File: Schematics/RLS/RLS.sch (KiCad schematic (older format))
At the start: 3 parts

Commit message: Updated schematic
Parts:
- added 1.5A: Fuse_Small2, symbol Fuse_Small
- added 1A: Fuse_Small3, symbol Fuse_Small
- added 4A: Fuse_Small1, symbol Fuse_Small
- added Arduino_Connector: ARDUINO_MEGA_SHIELD, symbol ARDUINO_MEGA_SHIELD
- added Logic_Analyzer_2: CONN_02X20, symbol CONN_02X20
- added Power_Supply: DIN_5, symbol DIN_5
- added R1, R10, R2, R3, R4, R5, R6, R7, R8, R9: 4.7K, symbol R
- added U1: ULN2803A, symbol ULN2803A
- added Voltmeter: CONN_01X10, symbol CONN_01X10
- gave numbers to parts that had none: 2
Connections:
- net labels added: AA12, AA13, AA14, AA15, AD10, AD11, AD12, AD13, AD22, AD23, AD24, AD25, AD26, AD27, AD28, AD29, AD30, AD31, AD32, AD33, AD34, AD35, AD36, AD37, AD38, AD39, AD4, AD40, AD41, AD42, AD43, AD44, AD45, AD46, AD47, AD5, AD6, AD7, AD8, AD9, GNDA, GNDD, L1CLK1, L1CLK2, L1D0, L1D1, L1D10, L1D11, L1D12, L1D13, L1D14, L1D15, L1D16, L1D17, L1D18, L1D19, L1D2, L1D20, L1D21, L1D22, L1D23, L1D24, L1D25, L1D26, L1D27, L1D28, L1D29, L1D3, L1D30, L1D31, L1D4, L1D5, L1D6, L1D7, L1D8, L1D9, L1GND, L2CLK1, L2CLK2, L2D0, L2D1, L2D10, L2D11, L2D12, L2D13, L2D14, L2D15, L2D16, L2D17, L2D18, L2D19, L2D2, L2D20, L2D21, L2D22, L2D23, L2D24, L2D25, L2D26, L2D27, L2D28, L2D29, L2D3, L2D30, L2D31, L2D4, L2D5, L2D6, L2D7, L2D8, L2D9, L2GND, RLY1, RLY2, SCL, SDA
- net labels removed: A14, A15, CLK1, CLK2, D0, D1, D10, D11, D12, D13, D14, D15, D16, D17, D18, D19, D2, D20, D21, D22, D23, D24, D25, D26, D27, D28, D29, D3, D30, D31, D32, D33, D34, D35, D36, D37, D38, D39, D4, D40, D41, D42, D43, D44, D45, D46, D47, D5, D6, D7, D8, D9, GND
- wire segments 0 -> 53
- no-connect marks 0 -> 15
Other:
- moved on the sheet: Arduino_Connector, BoardID_Regulator_Scope_Gen

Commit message: 06-23-2017 Update
Updated the scope probe network to it's own screen
Changed the connector setup
Fixed mirrored logic analyzer pins
Created voltage divider network for voltmeter
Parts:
- removed R1, R2: 4.7K, symbol R
- removed U1: ULN2803A, symbol ULN2803A
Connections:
- net labels added: VD01, VD02, VD03
- net labels removed: RLY1, RLY2, VM01, VM02, VM03
- wire segments 53 -> 46
- no-connect marks 15 -> 3
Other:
- note added: "VOLTMETER NOTES:\nVM00 MAX RANGE +/- 5V\nVD01 MAX RANGE +/- 10V\nVD02 MAX RANGE +/- 15V\nVD03 MAX RANGE +/- 15V"
- moved on the sheet: Logic_Analyzer_2

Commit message: 06-27-2017 Changes
Added positive and negative linear regulators (LT1963 and LT3015)
Added positive and negative regulator schematics (just placed items, still need to label everything)
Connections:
- wire segments 46 -> 53
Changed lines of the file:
@@
 $Descr A4 11693 8268
 encoding utf-8
-Sheet 1 3
+Sheet 1 5
 Title ""
 Date ""
@@
 L -15V #PWR?
 U 1 1 594B3412
-P 5750 7350
-F 0 "#PWR?" H 5750 7450 50  0001 C CNN
-F 1 "-15V" H 5750 7500 50  0000 C CNN
-F 2 "" H 5750 7350 50  0001 C CNN
-F 3 "" H 5750 7350 50  0001 C CNN
-	1    5750 7350
-	1    0    0    -1
-$EndComp
-Text GLabel 5750 7450 3    60   Input ~ 0
+P 5850 7350
+F 0 "#PWR?" H 5850 7450 50  0001 C CNN
+F 1 "-15V" H 5850 7500 50  0000 C CNN
+F 2 "" H 5850 7350 50  0001 C CNN
+F 3 "" H 5850 7350 50  0001 C CNN
+	1    5850 7350
+	1    0    0    -1
+$EndComp
+Text GLabel 5850 7450 3    60   Input ~ 0
 -15V
 Text GLabel 2600 3400 0    60   Input ~ 0
@@
 	1500 2300 1850 2300
 Wire Wire Line
-	1850 2300 1850 2600
+	1850 2300 1850 2450
+Wire Wire Line
+	1850 2450 1850 2600
 Wire Wire Line
 	1850 2600 1500 2600
@@
 	6250 7350 6250 7450
 Wire Wire Line
-	5750 7350 5750 7450
+	5850 7350 5850 7450
 Wire Wire Line
 	9400 2150 8750 2150
@@
 	8750 2850 8750 2800
 Wire Wire Line
-	8150 2850 8750 2850
+	8150 2850 8350 2850
+Wire Wire Line
+	8350 2850 8450 2850
+Wire Wire Line
+	8450 2850 8550 2850
+Wire Wire Line
+	8550 2850 8750 2850
 Wire Wire Line
 	8150 2850 8150 2800
@@
 	10500 2850 10500 2900
 Wire Wire Line
-	10500 2900 11100 2900
+	10500 2900 10700 2900
+Wire Wire Line
+	10700 2900 10800 2900
+Wire Wire Line
+	10800 2900 10900 2900
+Wire Wire Line
+	10900 2900 11100 2900
 Wire Wire Line
 	11100 2900 11100 2850
@@
 	9500 1600 9500 1050
 $Sheet
-S 1800 7200 500  500
+S 1700 7200 500  500
 U 594DCA38
 F0 "Scope_Probe_Gain" 60
 F1 "Scope_Probe_Gain.sch" 60
 $EndSheet
+$Sheet
+S 3000 7200 500  500
+U 5952F710
+F0 "Negative_Regulators" 60
+F1 "Negative_Regulators.sch" 60
+$EndSheet
+$Sheet
+S 4400 7200 500  500
+U 5952FCB2
+F0 "Positive_Regulators" 60
+F1 "Positive_Regulators.sch" 60
+$EndSheet
 $EndSCHEMATC

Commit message: Updated Regulator Circuits and Fixed Velleman Gain
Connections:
- net labels added: MOSI, N_POT_CE, P_POT_CE, SCLK
- wire segments 53 -> 46
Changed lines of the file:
@@
 EESchema Schematic File Version 2
+LIBS:RLS-rescue
 LIBS:power
 LIBS:device
@@
 SCL
 $Comp
-L GNDD #PWR?
+L GNDD #PWR01
 U 1 1 594B2EE5
 P 6450 7600
-F 0 "#PWR?" H 6450 7350 50  0001 C CNN
+F 0 "#PWR01" H 6450 7350 50  0001 C CNN
 F 1 "GNDD" H 6450 7450 50  0000 C CNN
 F 2 "" H 6450 7600 50  0001 C CNN
@@
 $EndComp
 $Comp
-L GNDA #PWR?
+L GNDA #PWR02
 U 1 1 594B2F17
 P 6700 7600
-F 0 "#PWR?" H 6700 7350 50  0001 C CNN
+F 0 "#PWR02" H 6700 7350 50  0001 C CNN
 F 1 "GNDA" H 6700 7450 50  0000 C CNN
 F 2 "" H 6700 7600 50  0001 C CNN
@@
 AGND
 $Comp
-L +5V #PWR?
+L +5V #PWR03
 U 1 1 594B303F
 P 6250 7350
-F 0 "#PWR?" H 6250 7200 50  0001 C CNN
+F 0 "#PWR03" H 6250 7200 50  0001 C CNN
 F 1 "+5V" H 6250 7490 50  0000 C CNN
 F 2 "" H 6250 7350 50  0001 C CNN
@@
 $EndComp
 $Comp
-L +15V #PWR?
+L +15V #PWR04
 U 1 1 594B3067
 P 6050 7350
-F 0 "#PWR?" H 6050 7200 50  0001 C CNN
+F 0 "#PWR04" H 6050 7200 50  0001 C CNN
 F 1 "+15V" H 6050 7490 50  0000 C CNN
 F 2 "" H 6050 7350 50  0001 C CNN
@@
 	1500 2300 1850 2300
 Wire Wire Line
-	1850 2300 1850 2450
-Wire Wire Line
-	1850 2450 1850 2600
+	1850 2300 1850 2600
 Wire Wire Line
 	1850 2600 1500 2600
@@
 	8750 2850 8750 2800
 Wire Wire Line
-	8150 2850 8350 2850
-Wire Wire Line
-	8350 2850 8450 2850
-Wire Wire Line
-	8450 2850 8550 2850
-Wire Wire Line
-	8550 2850 8750 2850
+	8150 2850 8750 2850
 Wire Wire Line
 	8150 2850 8150 2800
@@
 	10500 2850 10500 2900
 Wire Wire Line
-	10500 2900 10700 2900
-Wire Wire Line
-	10700 2900 10800 2900
-Wire Wire Line
-	10800 2900 10900 2900
-Wire Wire Line
-	10900 2900 11100 2900
+	10500 2900 11100 2900
 Wire Wire Line
 	11100 2900 11100 2850
@@
 F1 "Positive_Regulators.sch" 60
 $EndSheet
+Text GLabel 2600 4200 0    60   Input ~ 0
+N_POT_CE
+Text GLabel 2600 4500 0    60   Input ~ 0
+P_POT_CE
+Text GLabel 2600 4300 0    60   Input ~ 0
+SCLK
+Text GLabel 2600 4400 0    60   Input ~ 0
+MOSI
 $EndSCHEMATC

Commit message: Updated Schematic (Almost Done)
Finished both variable regulator circuits, added connectors for LAs, added +/- 5 regulated circuit for DB +/- 5V (needs to be tested before PCB implementation), various renaming and labeling
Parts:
- DB1: renamed from BoardID_Regulator_Scope_Gen; value CONN_02X20 -> BoardID_VIN_Scope_FuncGen_DB_CONN
- DB2: renamed from Arduino_Connector; value CONN_02X20 -> Arduino_DB_CONN
- DB3: renamed from Logic_Analyzer_1; value CONN_02X20 -> Logic_Analyzer1_DB_CONN
- DB4: renamed from Logic_Analyzer_2; value CONN_02X20 -> Logic_Analyzer2_DB_CONN
- F1: renamed from 1A; value Fuse_Small3 -> 1A
- F2: renamed from 1.5A; value Fuse_Small2 -> 1.5A
- F3: renamed from 4A; value Fuse_Small1 -> 4A
- J6: renamed from Voltmeter; value CONN_01X10 -> Voltmeter
- PSU1: renamed from Power_Supply; symbol DIN_5 -> DIN_5-RESCUE-RLS
- renumbered Arduino_Connector to U1
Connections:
- net labels added: +5V_R, +V1_SHDN, +V2_SHDN, -5V_R, -V1_SHDN, -V2_SHDN, VM01, VM02, VM03
- net labels removed: -5V
- wire segments 46 -> 61
- no-connect marks 3 -> 23
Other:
- note added: "VOLTMETER NOTES:\nVM00 MAX RANGE +/- 5V\nVM01 MAX RANGE +/- 10V\nVM02 MAX RANGE +/- 15V\nVM03 MAX RANGE +/- 15V"
- note removed: "VOLTMETER NOTES:\nVM00 MAX RANGE +/- 5V\nVD01 MAX RANGE +/- 10V\nVD02 MAX RANGE +/- 15V\nVD03 MAX RANGE +/- 15V"
- moved on the sheet: F3, U1

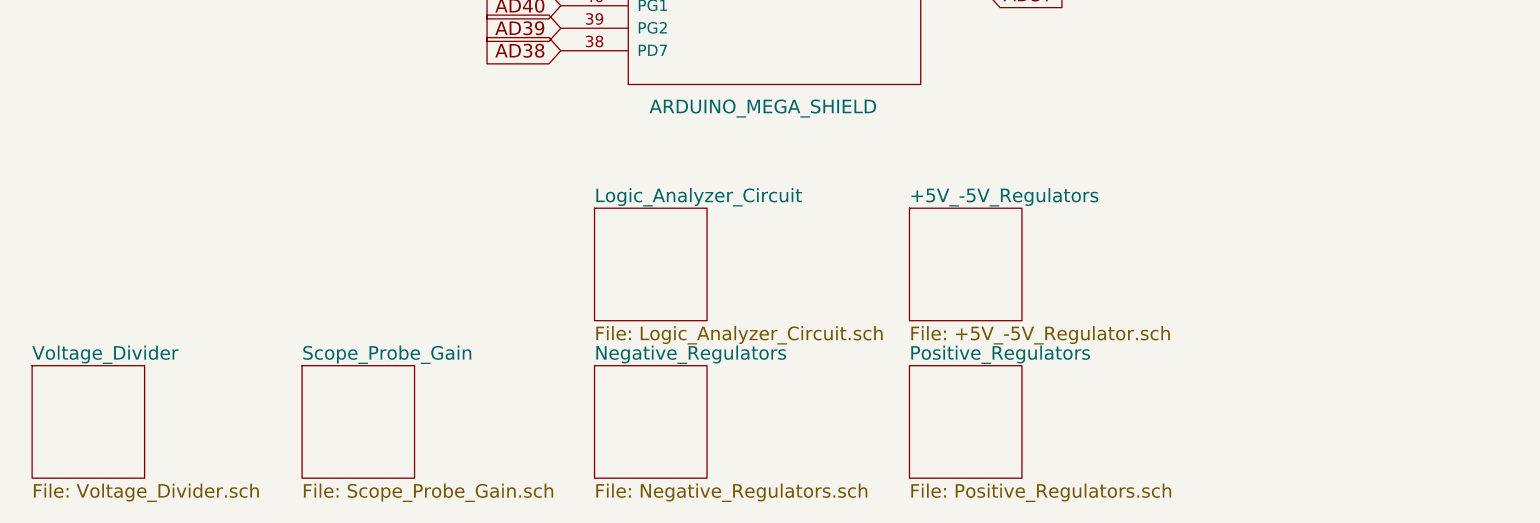
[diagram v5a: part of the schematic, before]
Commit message: Updated schematic (Complete)
Added fan circuit, updated +/- 5V regulated to have 1K pots. Next step is to truly begin the PCB. Will try to have completed by Friday. This will affect our schedule, but we can make up for it in ordering time ¯\_(ツ)_/¯
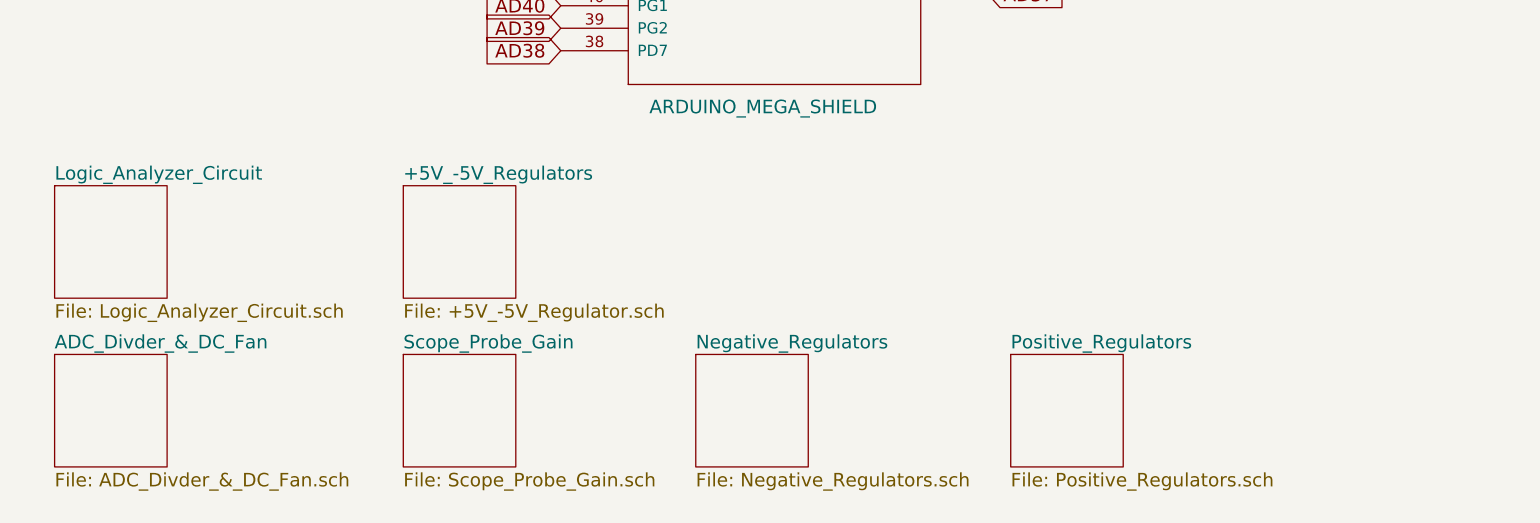
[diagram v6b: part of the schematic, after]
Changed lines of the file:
@@
 +5V
 $Sheet
-S 500  7200 500  500
+S 600  7150 500  500
 U 594D69D7
-F0 "Voltage_Divider" 60
-F1 "Voltage_Divider.sch" 60
+F0 "ADC_Divder_&_DC_Fan" 60
+F1 "ADC_Divder_&_DC_Fan.sch" 60
 $EndSheet
 Text Notes 9550 1550 0    60   ~ 0
 VOLTMETER NOTES:\nVM00 MAX RANGE +/- 5V\nVM01 MAX RANGE +/- 10V\nVM02 MAX RANGE +/- 15V\nVM03 MAX RANGE +/- 15V
 $Sheet
-S 1700 7200 500  500
+S 2150 7150 500  500
 U 594DCA38
 F0 "Scope_Probe_Gain" 60
@@
 $EndSheet
 $Sheet
-S 3000 7200 500  500
+S 3450 7150 500  500
 U 5952F710
 F0 "Negative_Regulators" 60
@@
 $EndSheet
 $Sheet
-S 4400 7200 500  500
+S 4850 7150 500  500
 U 5952FCB2
 F0 "Positive_Regulators" 60
@@
 -V2_SHDN
 $Sheet
-S 4400 6500 500  500
+S 2150 6400 500  500
 U 5959581C
 F0 "+5V_-5V_Regulators" 60
@@
 NoConn ~ 4750 1100
 $Sheet
-S 3000 6500 500  500
+S 600  6400 500  500
 U 595AF7B8
 F0 "Logic_Analyzer_Circuit" 60
@@
 $EndComp
 $Comp
-L +15V-RESCUE-RLS #PWR01
+L +15V-RESCUE-RLS #PWR3
 U 1 1 595A0DC0
 P 1600 700
-F 0 "#PWR01" H 1600 550 50  0001 C CNN
+F 0 "#PWR3" H 1600 550 50  0001 C CNN
 F 1 "+15V" H 1600 840 50  0000 C CNN
 F 2 "" H 1600 700 50  0001 C CNN
@@
 $EndComp
 $Comp
-L +5V-RESCUE-RLS #PWR02
+L +5V-RESCUE-RLS #PWR5
 U 1 1 595A0E0A
 P 2650 750
-F 0 "#PWR02" H 2650 600 50  0001 C CNN
+F 0 "#PWR5" H 2650 600 50  0001 C CNN
 F 1 "+5V" H 2650 890 50  0000 C CNN
 F 2 "" H 2650 750 50  0001 C CNN
@@
 $EndComp
 $Comp
-L GNDA-RESCUE-RLS #PWR03
+L GNDA-RESCUE-RLS #PWR4
 U 1 1 595A1070
 P 1950 950
-F 0 "#PWR03" H 1950 700 50  0001 C CNN
+F 0 "#PWR4" H 1950 700 50  0001 C CNN
 F 1 "GNDA" H 1950 800 50  0000 C CNN
 F 2 "" H 1950 950 50  0001 C CNN
@@
 $EndComp
 $Comp
-L GNDD-RESCUE-RLS #PWR04
+L GNDD-RESCUE-RLS #PWR2
 U 1 1 595A10A8
 P 1250 1600
-F 0 "#PWR04" H 1250 1350 50  0001 C CNN
+F 0 "#PWR2" H 1250 1350 50  0001 C CNN
 F 1 "GNDD" H 1250 1450 50  0000 C CNN
 F 2 "" H 1250 1600 50  0001 C CNN

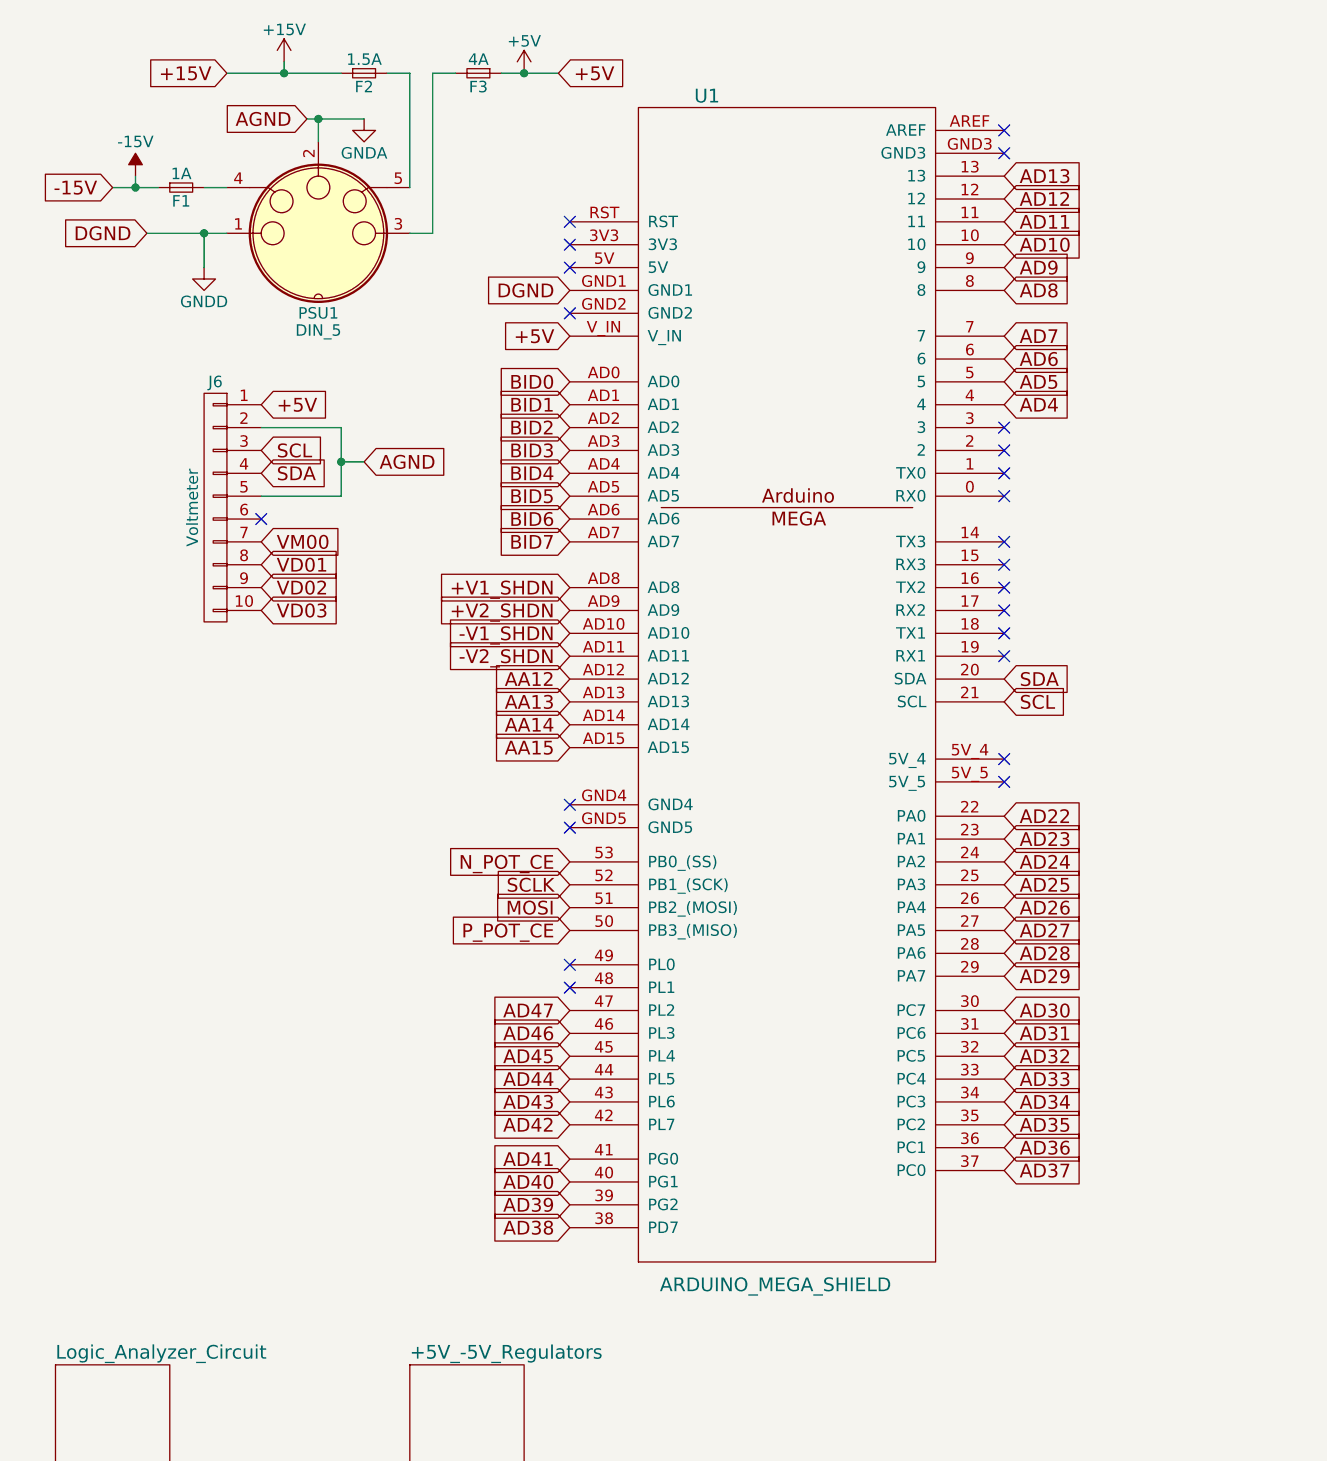
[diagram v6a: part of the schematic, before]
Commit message: Most Footprints Added
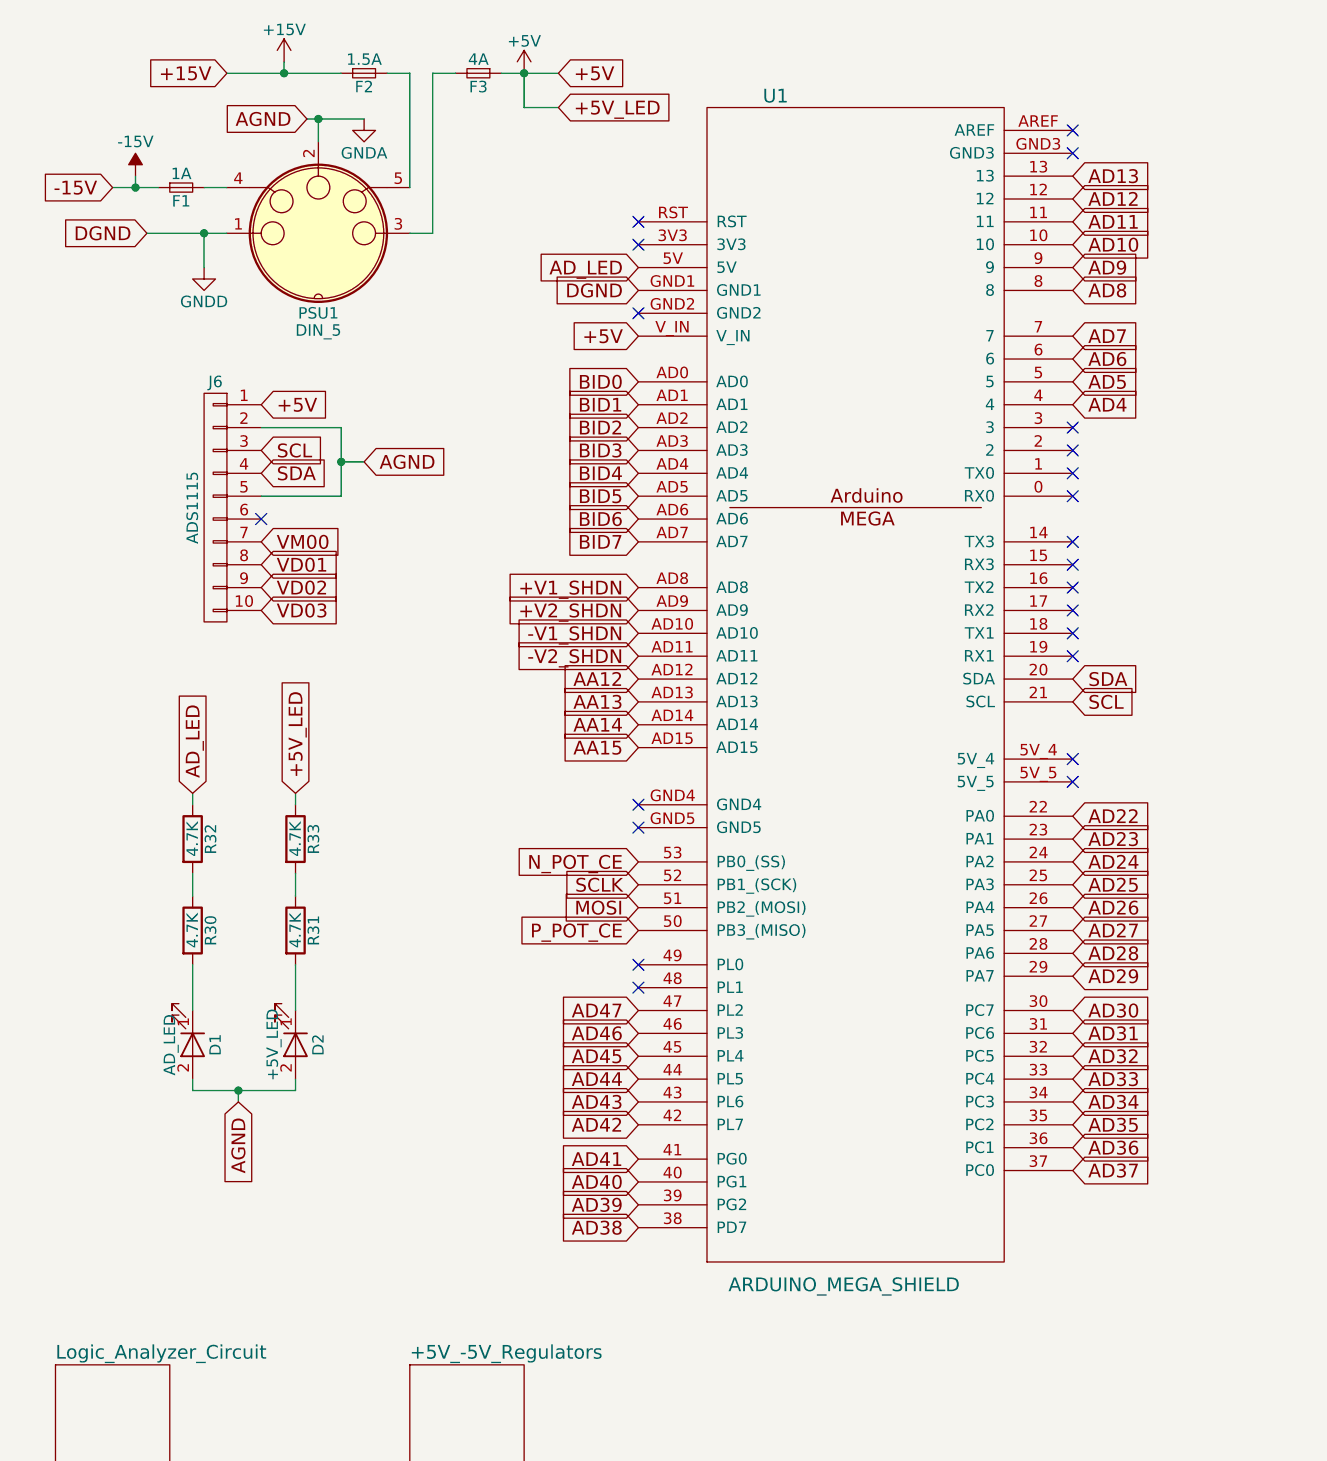
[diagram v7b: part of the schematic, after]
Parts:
- added D1: AD_LED, LEDs:LED_0603, symbol LED
- added D2: +5V_LED, LEDs:LED_0603, symbol LED
- added R30, R31, R32, R33: 4.7K, Resistors_SMD:R_0805_HandSoldering, symbol R
- DB1, DB2, DB3, DB4: footprint (none) -> Pin_Headers:Pin_Header_Straight_2x20_Pitch2.54mm
- F1, F2, F3: footprint (none) -> Fuse_Holders_and_Fuses:Fuse_SMD2920
- J6: value Voltmeter -> ADS1115; footprint (none) -> Pin_Headers:Pin_Header_Straight_1x10_Pitch2.54mm
- R10, R3, R4, R5, R6, R7, R8, R9: footprint (none) -> Resistors_SMD:R_0805_HandSoldering
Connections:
- net +5V: now also R33.1
- net AGND: now also D1.2 (A), D2.2 (A)
- net AD_LED: now reaches U1.5V
- net AD_LED: now also R32.1
- new net: D1.1 (K), R30.2
- new net: D2.1 (K), R31.2
- new net: R30.1, R32.2
- new net: R31.1, R33.2
- no-connect marks 23 -> 22
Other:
- moved on the sheet: U1
